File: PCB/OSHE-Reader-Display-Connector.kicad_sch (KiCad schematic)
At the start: 18 parts, among them J3 Conn_01x24_MountingPin, Q1 Si1308EDL

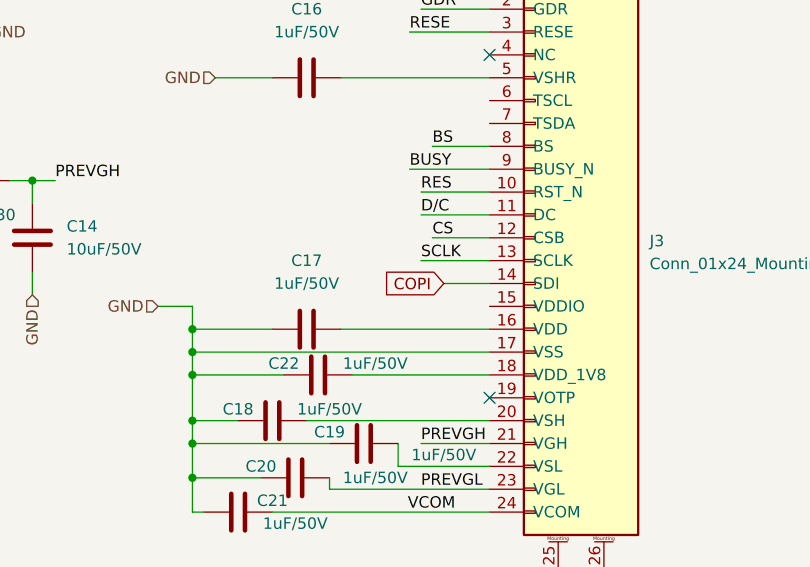
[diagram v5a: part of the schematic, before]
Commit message: Updating pins in roots file
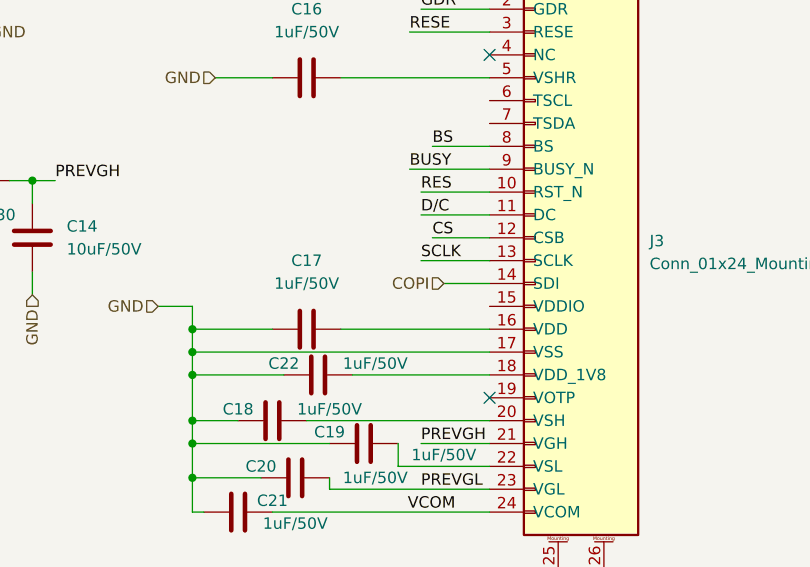
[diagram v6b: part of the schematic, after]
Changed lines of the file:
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@@
-		)
-	)
-	(global_label "COPI"
-		(shape input)
-		(at 116.84 71.12 180)
-		(fields_autoplaced yes)
-		(effects
-			(font
-				(size 1.27 1.27)
-			)
-			(justify right)
-		)
-		(property "Intersheetrefs" "${INTERSHEET_REFS}"
-			(at 109.3795 71.12 0)
-			(effects
-				(font
-					(size 1.27 1.27)
-				)
-				(justify right)
-				(hide yes)
-			)
 		)
 	)
@@
 		(effects
 			(font
+				(size 1.27 1.27)
+			)
+			(justify right)
+		)
+	)
+	(hierarchical_label "COPI"
+		(shape input)
+		(at 116.84 71.12 180)
+		(effects
+			(font

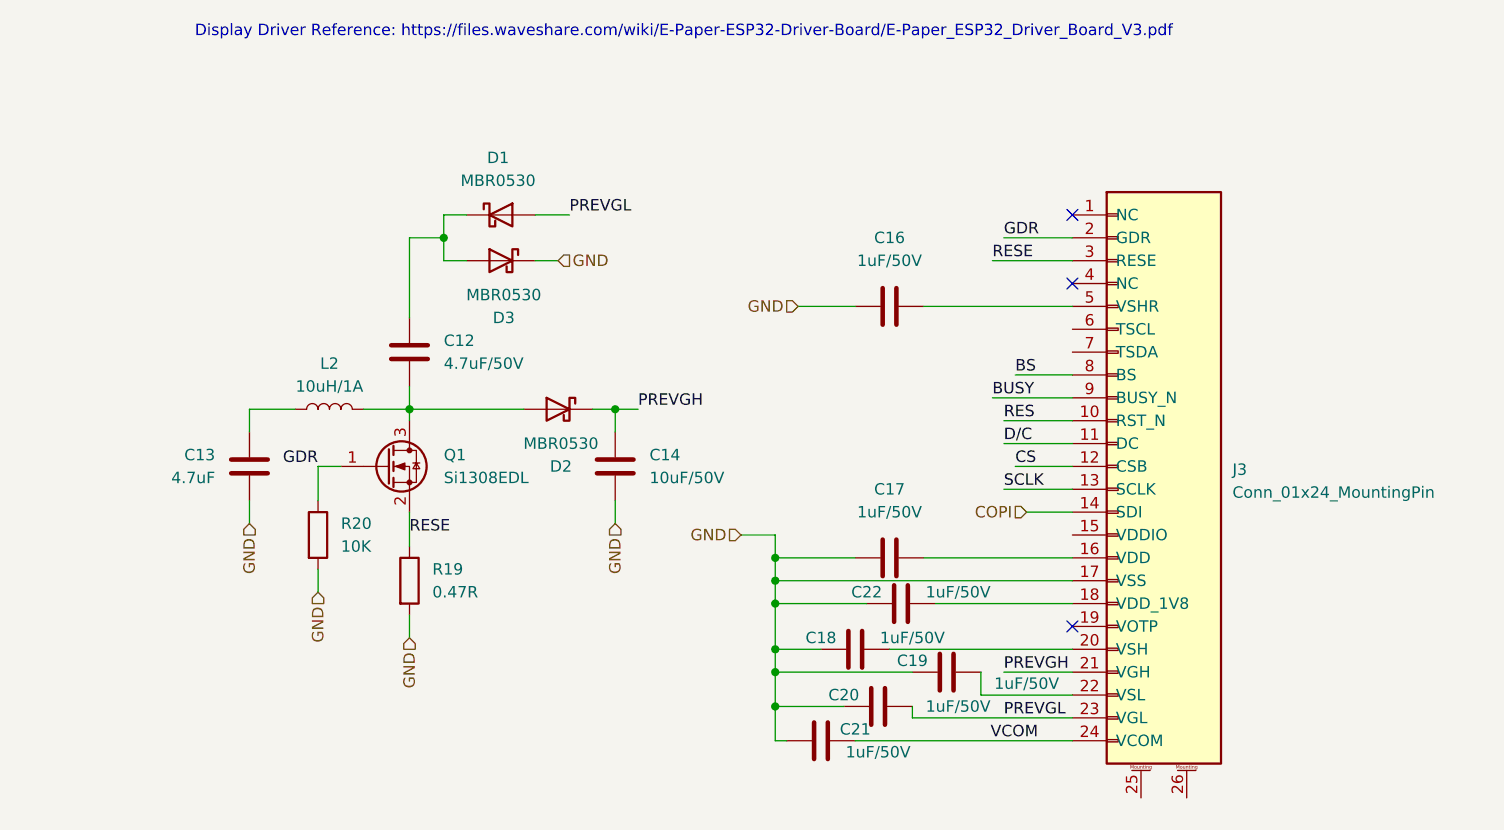
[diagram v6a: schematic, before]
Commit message: Update OSHE-Reader-Display-Connector.kicad_sch
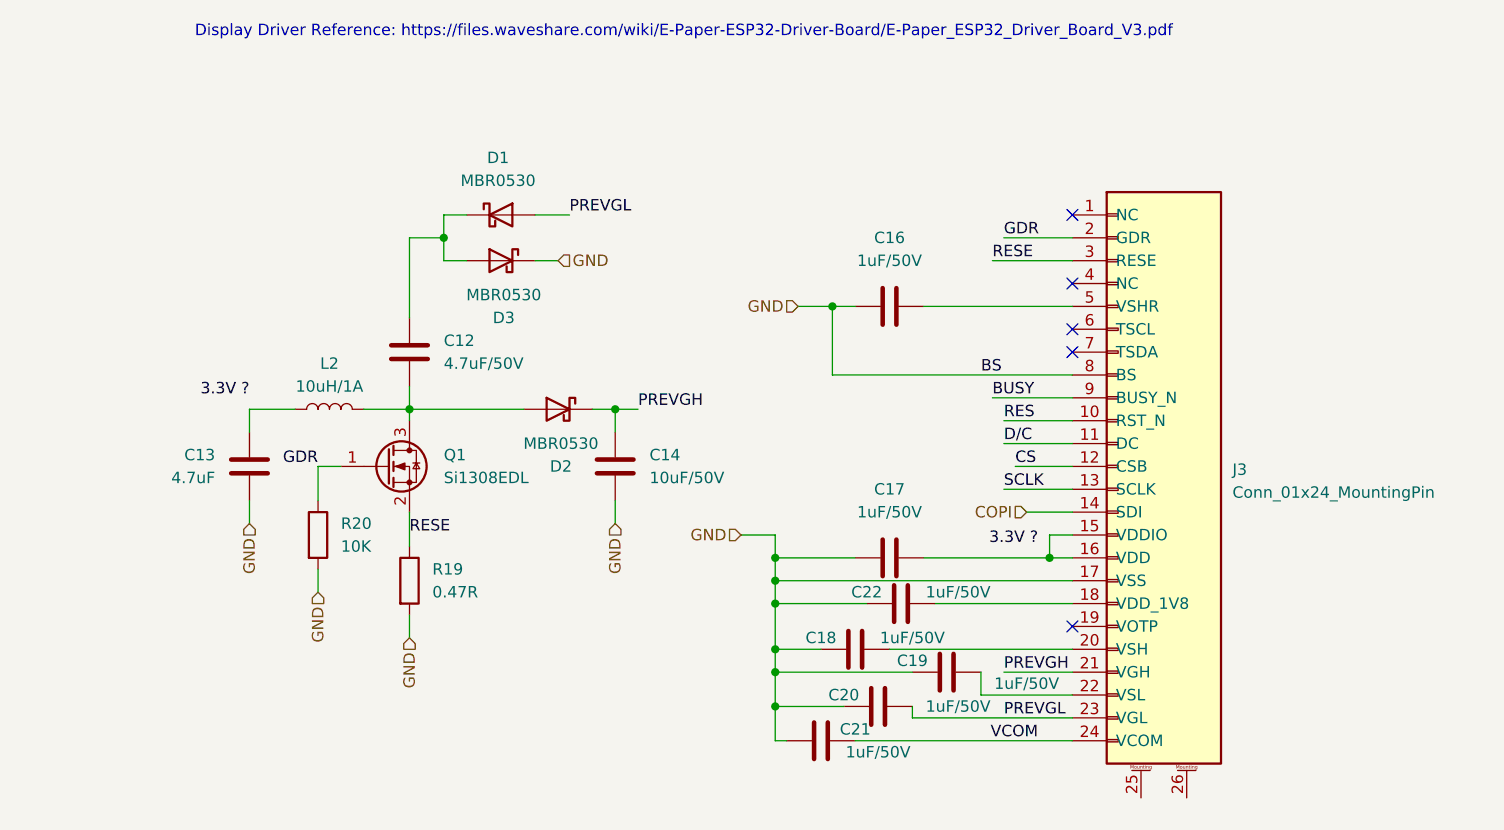
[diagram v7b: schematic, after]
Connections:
- net BS is gone; now on net GND: J3.8 (BS)
- net at J3.15 (VDDIO): now also C17.1, J3.16 (VDD)
- no-connect marks 3 -> 5
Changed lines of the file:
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@@
 				(size 1.27 1.27)
 			)
-		)
+			(href "https://files.waveshare.com/wiki/E-Paper-ESP32-Driver-Board/E-Paper_ESP32_Driver_Board_V3.pdf")
+		)
+	)
+	(junction
+		(at 119.38 76.2)
+		(diameter 0)
+		(color 0 0 0 0)
 	)
 	(junction
@@
 	(junction
 		(at 88.9 76.2)
+		(diameter 0)
+		(color 0 0 0 0)
+	)
+	(junction
+		(at 95.25 48.26)
 		(diameter 0)
 		(color 0 0 0 0)
@@
 	)
 	(no_connect
+		(at 121.92 53.34)
+	)
+	(no_connect
+		(at 121.92 50.8)
+	)
+	(no_connect
 		(at 121.92 83.82)
 	)
@@
 	(wire
 		(pts
+			(xy 121.92 55.88) (xy 95.25 55.88)
+		)
+		(stroke
+			(width 0)
+			(type default)
+		)
+	)
+	(wire
+		(pts
 			(xy 71.12 59.69) (xy 73.66 59.69)
 		)
@@
 	(wire
 		(pts
+			(xy 119.38 76.2) (xy 121.92 76.2)
+		)
+		(stroke
+			(width 0)
+			(type default)
+		)
+	)
+	(wire
+		(pts
 			(xy 88.9 88.9) (xy 104.14 88.9)
 		)
@@
 	(wire
 		(pts
+			(xy 121.92 73.66) (xy 119.38 73.66)
+		)
+		(stroke
+			(width 0)
+			(type default)
+		)
+	)
+	(wire
+		(pts
 			(xy 114.3 63.5) (xy 121.92 63.5)
 		)
@@
 	(wire
 		(pts
-			(xy 115.57 55.88) (xy 121.92 55.88)
-		)
-		(stroke
-			(width 0)
-			(type default)
-		)
-	)
-	(wire
-		(pts
 			(xy 52.07 40.64) (xy 52.07 43.18)
 		)
@@
 	(wire
 		(pts
+			(xy 119.38 73.66) (xy 119.38 76.2)
+		)
+		(stroke
+			(width 0)
+			(type default)
+		)
+	)
+	(wire
+		(pts
 			(xy 52.07 43.18) (xy 54.61 43.18)
 		)
@@
 	(wire
 		(pts
+			(xy 95.25 55.88) (xy 95.25 48.26)
+		)
+		(stroke
+			(width 0)
+			(type default)
+		)
+	)
+	(wire
+		(pts
 			(xy 97.79 96.52) (xy 121.92 96.52)
 		)
@@
 	(wire
 		(pts
-			(xy 91.44 48.26) (xy 97.79 48.26)
+			(xy 91.44 48.26) (xy 95.25 48.26)
 		)
 		(stroke
@@
 	(wire
 		(pts
+			(xy 95.25 48.26) (xy 97.79 48.26)
+		)
+		(stroke
+			(width 0)
+			(type default)
+		)
+	)
+	(wire
+		(pts
 			(xy 66.04 38.1) (xy 62.23 38.1)
 		)
@@
 	(wire
 		(pts
-			(xy 105.41 76.2) (xy 121.92 76.2)
+			(xy 105.41 76.2) (xy 119.38 76.2)
 		)
 		(stroke
@@
 		)
 	)
+	(label "3.3V ?"
+		(at 30.48 58.42 180)
+		(effects
+			(font
+				(size 1.27 1.27)
+			)
+			(justify right bottom)
+		)
+	)
 	(label "PREVGL"
 		(at 66.04 38.1 0)
@@
 		)
 	)
+	(label "3.3V ?"
+		(at 118.11 74.93 180)
+		(effects
+			(font
+				(size 1.27 1.27)
+			)
+			(justify right bottom)
+		)
+	)
 	(label "RESE"
 		(at 113.03 43.18 0)
@@
 	)
 	(label "BS"
-		(at 115.57 55.88 0)
-		(effects
-			(font
+		(at 111.76 55.88 0)
+		(effects
+			(font

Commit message: Update OSHE-Reader-Display-Connector.kicad_sch
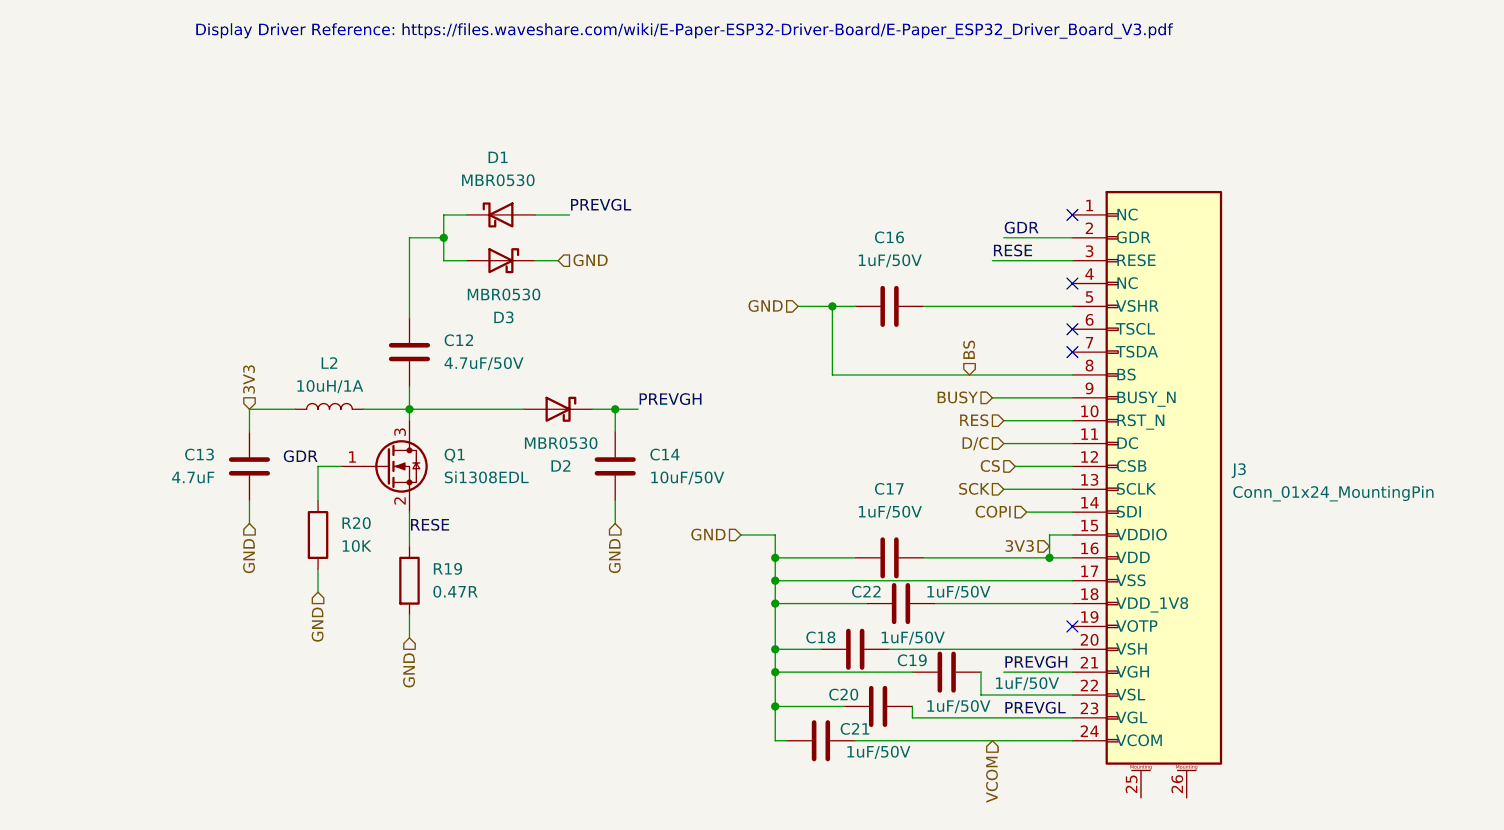
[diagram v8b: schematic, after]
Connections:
- net 3V3: now reaches C17.1, J3.15 (VDDIO), J3.16 (VDD)
- net 3V3: now also C13.1, L2.1
- net GND renamed BS
- net SCLK renamed SCK
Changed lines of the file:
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@@
-		)
-	)
-	(label "SCLK"
-		(at 114.3 68.58 0)
-		(effects
-			(font
-				(size 1.27 1.27)
-			)
-			(justify left bottom)
 		)
 	)
@@
 		)
 	)
-	(label "RES"
-		(at 114.3 60.96 0)
-		(effects
-			(font
-				(size 1.27 1.27)
-			)
-			(justify left bottom)
-		)
-	)
 	(label "PREVGL"
 		(at 114.3 93.98 0)
@@
 		)
 	)
-	(label "CS"
-		(at 115.57 66.04 0)
-		(effects
-			(font
-				(size 1.27 1.27)
-			)
-			(justify left bottom)
-		)
-	)
-	(label "3.3V ?"
-		(at 30.48 58.42 180)
-		(effects
-			(font
-				(size 1.27 1.27)
-			)
-			(justify right bottom)
-		)
-	)
 	(label "PREVGL"
 		(at 66.04 38.1 0)
@@
 		)
 	)
-	(label "BUSY"
-		(at 113.03 58.42 0)
-		(effects
-			(font
-				(size 1.27 1.27)
-			)
-			(justify left bottom)
-		)
-	)
-	(label "D{slash}C"
-		(at 114.3 63.5 0)
-		(effects
-			(font
-				(size 1.27 1.27)
-			)
-			(justify left bottom)
-		)
-	)
-	(label "VCOM"
-		(at 118.11 96.52 180)
-		(effects
-			(font
-				(size 1.27 1.27)
-			)
-			(justify right bottom)
-		)
-	)
-	(label "3.3V ?"
-		(at 118.11 74.93 180)
-		(effects
-			(font
-				(size 1.27 1.27)
-			)
-			(justify right bottom)
-		)
-	)
 	(label "RESE"
 		(at 113.03 43.18 0)
@@
 		)
 	)
-	(label "BS"
-		(at 111.76 55.88 0)
-		(effects
-			(font
-				(size 1.27 1.27)
-			)
-			(justify left bottom)
+	(hierarchical_label "D{slash}C"
+		(shape input)
+		(at 114.3 63.5 180)
+		(effects
+			(font
+				(size 1.27 1.27)
+			)
+			(justify right)
+		)
+	)
+	(hierarchical_label "3V3"
+		(shape input)
+		(at 119.38 74.93 180)
+		(effects
+			(font
+				(size 1.27 1.27)
+			)
+			(justify right)
 		)
 	)
@@
 		)
 	)
+	(hierarchical_label "CS"
+		(shape input)
+		(at 115.57 66.04 180)
+		(effects
+			(font
+				(size 1.27 1.27)
+			)
+			(justify right)
+		)
+	)
+	(hierarchical_label "RES"
+		(shape input)
+		(at 114.3 60.96 180)
+		(effects
+			(font
+				(size 1.27 1.27)
+			)
+			(justify right)
+		)
+	)
+	(hierarchical_label "BS"
+		(shape input)
+		(at 110.49 55.88 90)
+		(effects
+			(font
+				(size 1.27 1.27)
+			)
+			(justify left)
+		)
+	)
+	(hierarchical_label "BUSY"
+		(shape input)
+		(at 113.03 58.42 180)
+		(effects
+			(font
+				(size 1.27 1.27)
+			)
+			(justify right)
+		)
+	)
 	(hierarchical_label "GND"
 		(shape input)
@@
 		)
 	)
+	(hierarchical_label "SCK"
+		(shape input)
+		(at 114.3 68.58 180)
+		(effects
+			(font
+				(size 1.27 1.27)
+			)
+			(justify right)
+		)
+	)
+	(hierarchical_label "VCOM"
+		(shape input)
+		(at 113.03 96.52 270)
+		(effects
+			(font
+				(size 1.27 1.27)
+			)
+			(justify right)
+		)
+	)
+	(hierarchical_label "3V3"
+		(shape input)
+		(at 30.48 59.69 90)
+		(effects
+			(font
+				(size 1.27 1.27)
+			)
+			(justify left)
+		)
+	)
